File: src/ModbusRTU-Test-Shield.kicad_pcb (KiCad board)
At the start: 2 copper layers, 68.6 x 53.3 mm, 46 parts, among them J1 Conn_01x08_UNO_Digital_1, J2 Conn_01x10_UNO_Digital_2, J3 Conn_01x08_UNO_Power, J4 Conn_01x06_UNO_Analog, J5 Screw_Terminal_01x03, J6 6P6C, SW1 RESET, SW2 BUTTON1, SW3 BUTTON2, SW4 SW_DPDT_x2, U1 LT1785AxN8, U2 MAX232

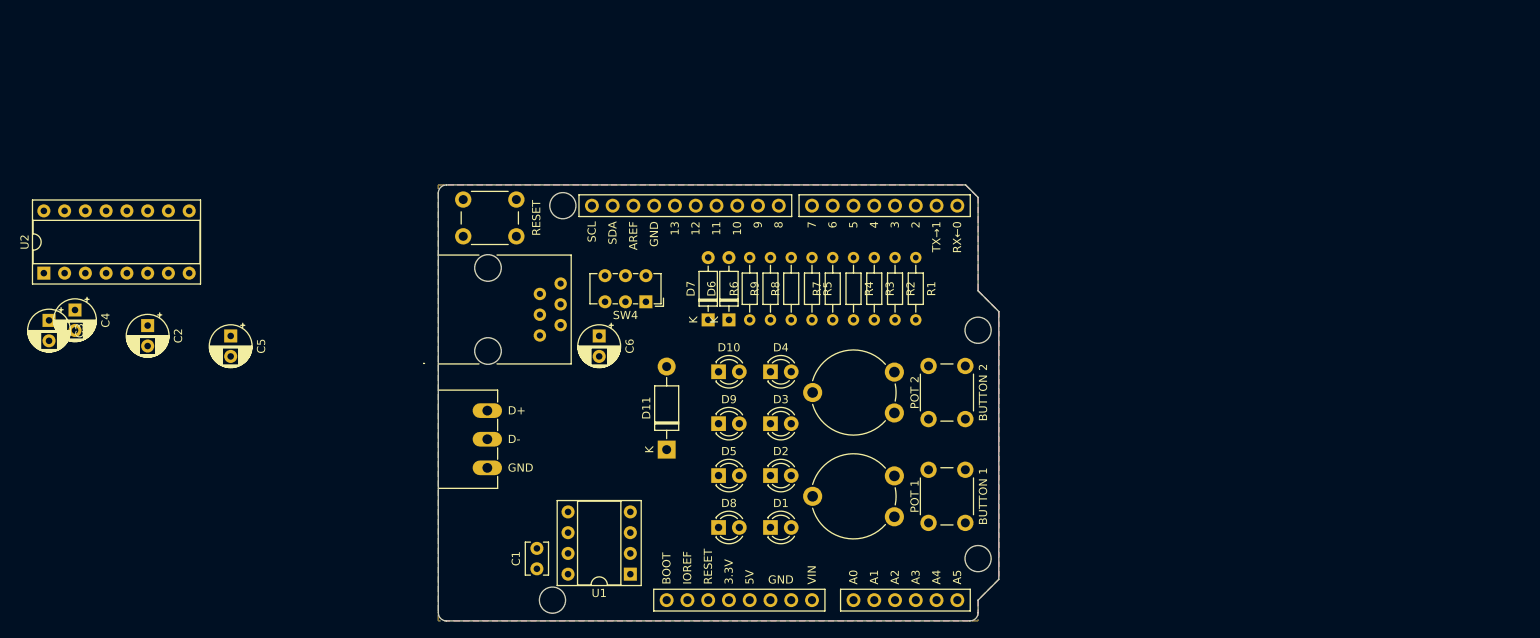
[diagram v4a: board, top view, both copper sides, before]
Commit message: Updated the schematic and board to use the new footprints and models.
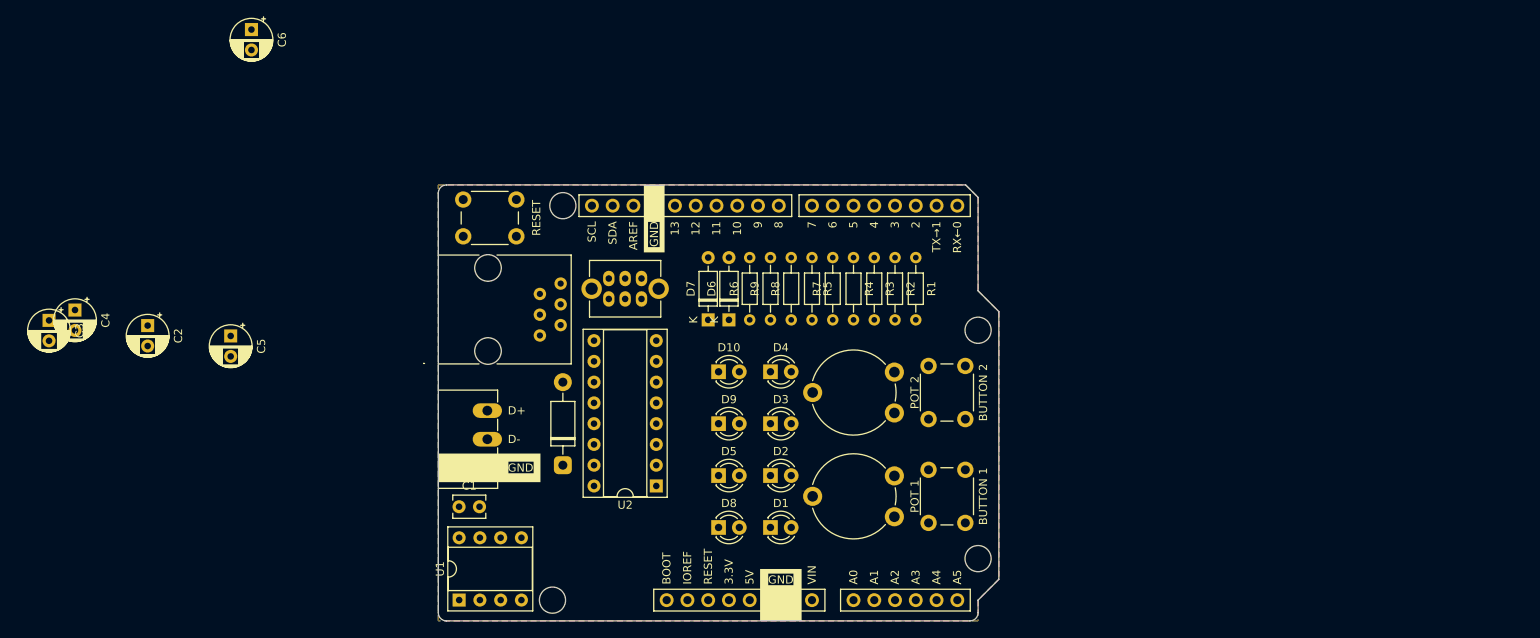
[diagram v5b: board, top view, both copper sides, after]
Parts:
- D11: footprint Diode_THT:D_DO-41_SOD81_P10.16mm_Horizontal -> Project_Footprints:D_DO-41_SOD81_P10.16mm_Horizontal
- SW4: footprint Button_Switch_THT:SW_E-Switch_EG1271_SPDT -> Project_Footprints:SW_CK_OS202011MS2Qx1_DPDT
- moved U2 79.3 mm to (132.1, 118.1), turned to 180 degrees
- moved C6 56.7 mm to (82.5, 62.3)
- moved U1 21.2 mm to (108.0, 132.1), turned to 90 degrees
- moved D11 12.8 mm to (120.7, 115.6)
- moved C1 12.2 mm to (108.0, 120.7), turned to 0 degrees
- moved SW4 3.00 mm to (128.3, 94.0)

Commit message: Completed third draft.
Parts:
- removed C1: 0.1uF, Capacitor_THT:C_Disc_D3.8mm_W2.6mm_P2.50mm
- C2, C3, C4, C5, C6: footprint Capacitor_THT:CP_Radial_D5.0mm_P2.50mm -> Project_Footprints:CP_Radial_D5.0mm_P2.50mm
- D1, D10, D2, D3, D4, D5, D8, D9: footprint LED_THT:LED_D3.0mm -> Project_Footprints:LED_D3.0mm
- D6, D7: footprint Diode_THT:D_DO-35_SOD27_P7.62mm_Horizontal -> Project_Footprints:D_DO-35_SOD27_P7.62mm_Horizontal
- R1, R2, R3, R4, R5, R6, R7, R8, R9: footprint Resistor_THT:R_Axial_DIN0204_L3.6mm_D1.6mm_P7.62mm_Horizontal -> Project_Footprints:R_Axial_DIN0204_L3.6mm_D1.6mm_P7.62mm_Horizontal
- U1: value LT1785AxN8 -> LT1785; footprint Package_DIP:DIP-8_W7.62mm_Socket -> Project_Footprints:DIP-8_W7.62mm_Socket
- U2: footprint Package_DIP:DIP-16_W7.62mm_Socket -> Project_Footprints:DIP-16_W7.62mm_Socket
- moved C3 78.0 mm to (132.7, 119.4), turned to 90 degrees
- moved C6 76.6 mm to (122.6, 127.6)
- moved C4 74.7 mm to (128.9, 127.6)
- moved C2 64.5 mm to (132.7, 113.0), turned to 90 degrees
- moved C5 53.2 mm to (132.7, 106.7)
- moved D11 24.3 mm to (123.8, 91.4), turned to -90 degrees
- moved U2 6.36 mm to (128.3, 123.2)
- moved U1 3.86 mm to (108.6, 128.3)
- moved SW4 3.17 mm to (131.4, 94.0)
- moved D10 2.01 mm to (137.8, 103.5)
- moved D5 2.01 mm to (137.8, 116.2)
- moved D8 2.01 mm to (137.8, 122.6)
- moved D9 2.01 mm to (137.8, 109.9)
- moved D2 1.42 mm to (144.8, 116.2)
- moved D4 1.42 mm to (144.8, 103.5)
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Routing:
- net +5V: track 0.00 -> 103.8 mm
- net /IOREF: track 0.00 -> 91.9 mm
- net /RESET: track 0.00 -> 83.9 mm
- net /DE: track 0.00 -> 80.4 mm
- net /TX: track 0.00 -> 64.1 mm
- net Net-(D6-K): track 0.00 -> 55.1 mm
- net /BUTTON2: track 0.00 -> 49.3 mm
- net /HARD_RX: track 0.00 -> 42.5 mm
- net /HARD_TX: track 0.00 -> 39.7 mm
- net /BUTTON1: track 0.00 -> 39.0 mm
- net Net-(D1-A): track 0.00 -> 36.3 mm
- net Net-(D8-K): track 0.00 -> 35.7 mm
- net /POT2: track 0.00 -> 29.0 mm
- net Net-(D2-A): track 0.00 -> 27.7 mm
- net Net-(D5-A): track 0.00 -> 26.1 mm
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- removed copper zone on B.Cu, net GND

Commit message: Completed fourth draft.
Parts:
- added C1: 1uF, Project_Footprints:CP_Radial_D4.0mm_P1.50mm, F.Cu at (109.2, 127.6)
- C2: renamed from C6; footprint Project_Footprints:CP_Radial_D5.0mm_P2.50mm -> Project_Footprints:CP_Radial_D4.0mm_P1.50mm
- C3: renamed from C4; footprint Project_Footprints:CP_Radial_D5.0mm_P2.50mm -> Project_Footprints:CP_Radial_D4.0mm_P1.50mm
- C4: renamed from C3; footprint Project_Footprints:CP_Radial_D5.0mm_P2.50mm -> Project_Footprints:CP_Radial_D4.0mm_P1.50mm
- C5: footprint Project_Footprints:CP_Radial_D5.0mm_P2.50mm -> Project_Footprints:CP_Radial_D4.0mm_P1.50mm
- C6: renamed from C2; footprint Project_Footprints:CP_Radial_D5.0mm_P2.50mm -> Project_Footprints:CP_Radial_D4.0mm_P1.50mm
- D10: renamed from D7; value D_Schottky -> BAT43
- D11: value D_Schottky -> SB260S
- D9: renamed from D6; value D_Schottky -> BAT43
- J1: value Conn_01x08_UNO_Digital_1 -> SP-140520-08-001
- J2: value Conn_01x10_UNO_Digital_2 -> SP-140520-10-001
- J3: value Conn_01x08_UNO_Power -> SP-140520-08-001
- J4: value Conn_01x06_UNO_Analog -> SP-140520-06-001
- J5: value Screw_Terminal_01x03 -> 5430438
- J6: value 6P6C -> 54601-906WPLF
- SW4: value SW_DPDT_x2 -> OS202011MS2QN1
- moved REF** 67.6 mm to (143.5, 127.0)
- moved REF** 46.3 mm to (156.8, 125.7)
- moved C3 12.9 mm to (135.9, 116.8), turned to 90 degrees
- moved U1 12.1 mm to (120.7, 128.3), turned to 180 degrees
- moved C4 4.07 mm to (135.9, 121.9)
- moved U2 3.81 mm to (132.1, 123.2)
- moved D5 3.81 mm to (141.6, 122.6)
- moved D6 3.81 mm to (141.6, 116.2)
- moved D7 3.81 mm to (141.6, 109.9)
- moved D8 3.81 mm to (141.6, 103.5)
- moved C6 3.42 mm to (135.9, 111.8)
- moved D1 3.18 mm to (148.0, 122.6)
- moved D2 3.18 mm to (148.0, 116.2)
- moved D3 3.18 mm to (148.0, 109.9)
- moved D4 3.18 mm to (148.0, 103.5)
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- renumbered D8 to D5, D5 to D6, D9 to D7, D10 to D8, R7 to R5, R5 to R6, R8 to R7, R9 to R8, R6 to R9, SW2 to SW1, SW3 to SW2, SW1 to SW3
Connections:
- J1 pad 3: /BUTTON2 -> /BUTTON1
- J1 pad 4: /BUTTON1 -> /BUTTON2
- J1 pad 6: /LED4 -> /LED1
- J1 pad 7: /LED3 -> /LED2
- J1 pad 8: /LED2 -> /LED3
- J2 pad 1: /LED1 -> /LED4
- R1 pad 1: /LED4 -> /LED1
- R2 pad 1: /LED3 -> /LED2
- R3 pad 1: /LED2 -> /LED3
- R4 pad 1: /LED1 -> /LED4
- SW1 pad 1: /BUTTON2 -> /BUTTON1
- SW2 pad 1: /BUTTON1 -> /BUTTON2
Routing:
- net Net-(D9-K): track 55.1 -> 41.9 mm
- net /BUTTON2: track 49.3 -> 38.4 mm
- net /BUTTON1: track 39.0 -> 48.8 mm
- net /TX: track 64.1 -> 57.2 mm
- net /RS485_D-: track 10.1 -> 16.0 mm
- net /DE: track 80.4 -> 76.2 mm
- net Net-(D8-K): track 11.9 -> 8.08 mm
- net Net-(D10-K): track 26.1 -> 22.5 mm
- net Net-(D5-K): track 35.7 -> 32.5 mm
- net /RS485_D+: track 13.3 -> 16.5 mm
- net Net-(D4-A): track 12.5 -> 9.35 mm
- net Net-(D6-A): track 26.1 -> 23.2 mm
- net /RS232_TX: track 23.0 -> 25.8 mm
- net Net-(D7-K): track 18.6 -> 15.9 mm
- net +5V: track 103.8 -> 101.1 mm
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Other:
- board text added: "MODBUS"
- board text added: "RTU"
- board text removed: "MODBUS RTU"

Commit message: Updated the main source files.
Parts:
- U1: value LT1785 -> RS-485 XCVR
- U2: value MAX232 -> RS-232 XCVR
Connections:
- SW4 pad MP: (no net) -> GND
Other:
- board text added: "Circuit Board Specifications Board Thickness: 1.6mm Substrate Material: FR4 Copper Layers: 2 Copper Thickness: 1oz Soldermask Color: Any (Blue Suggested) Surface Finish: Any (HASL Lead-Free Suggested) Smallest Hole Diameter: 0.6mm Smallest Trace Width: 0.2mm (7.8mil) Smallest Trace Spacing: 0.2mm (7.8mil) Documentation and source files can be found at https://github.com/CMB27/ModbusRTU-Test-Shiel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"
- board text removed: "Circuit Board Specifications Board Thickness: 1.6mm Substrate Material: FR4 Copper Layers: 2 Copper Thickness: 1oz Soldermask Color: Any (Blue Suggested) Surface Finish: Any (HASL Lead-Free Suggested) Smallest Hole Diameter: 0.8mm Smallest Trace Width: 0.2mm (7.8mil) Smallest Trace Spacing: 0.2mm (7.8mil) Documentation and source files can be found at https://github.com/CMB27/ModbusRTU-Test-Shiel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"
